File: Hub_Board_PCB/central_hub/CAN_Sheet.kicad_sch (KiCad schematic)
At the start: 14 parts, among them J6 CAN_OUT, U1 MCP2515-xST, U2 TJA1050, Y1 20M

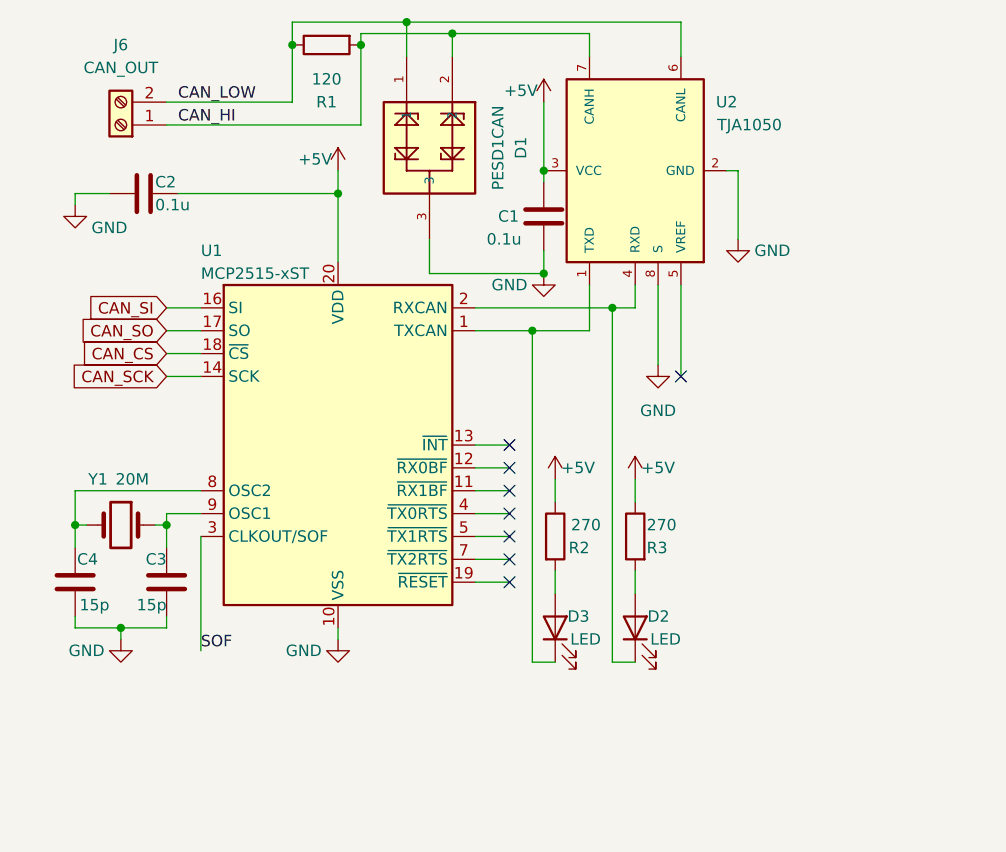
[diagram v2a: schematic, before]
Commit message: Added footprints for almost all components
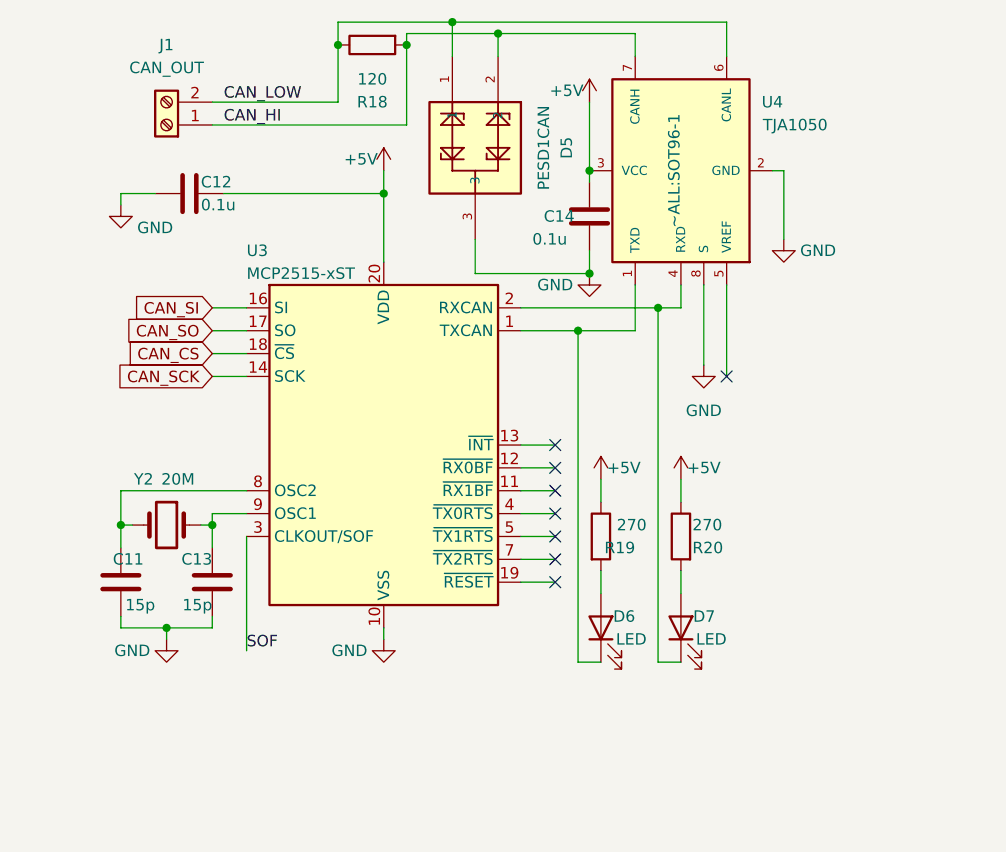
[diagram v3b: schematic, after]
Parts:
- removed C1, C2: 0.1u, Capacitor_SMD:C_0603_1608Metric, symbol Device:C
- removed C3, C4: 15p, Capacitor_SMD:C_0603_1608Metric, symbol Device:C
- removed D1: PESD1CAN, PESD1CAN:SOT23-3, symbol PESD1CAN:PESD1CAN
- removed D2, D3: LED, LED_SMD:LED_1206_3216Metric, symbol Device:LED
- removed J6: CAN_OUT, symbol Connector:Screw_Terminal_01x02
- removed R1: 120, Resistor_SMD:R_0603_1608Metric_Pad0.98x0.95mm_HandSolder, symbol Device:R
- removed R2, R3: 270, Resistor_SMD:R_0603_1608Metric_Pad0.98x0.95mm_HandSolder, symbol Device:R
- removed U1: MCP2515-xST, Package_SO:TSSOP-20_4.4x6.5mm_P0.65mm, symbol Interface_CAN_LIN:MCP2515-xST
- removed U2: TJA1050, TJA1050:SOT96-1, symbol TJA1050:TJA1050
- removed Y1: 20M, Crystal:Crystal_HC49-U_Vertical, symbol Device:Crystal
- added C11, C13: 15p, Capacitor_SMD:C_0603_1608Metric, symbol Device:C
- added C12, C14: 0.1u, Capacitor_SMD:C_0603_1608Metric, symbol Device:C
- added D5: PESD1CAN, ~ALL:SOT23-3, symbol PESD1CAN:PESD1CAN
- added D6, D7: LED, LED_SMD:LED_1206_3216Metric, symbol Device:LED
- added J1: CAN_OUT, Connector_PinHeader_2.54mm:PinHeader_1x02_P2.54mm_Vertical, symbol Connector:Screw_Terminal_01x02
- added R18: 120, Resistor_SMD:R_0603_1608Metric_Pad0.98x0.95mm_HandSolder, symbol Device:R
- added R19, R20: 270, Resistor_SMD:R_0603_1608Metric_Pad0.98x0.95mm_HandSolder, symbol Device:R
- added U3: MCP2515-xST, Package_SO:TSSOP-20_4.4x6.5mm_P0.65mm, symbol Interface_CAN_LIN:MCP2515-xST
- added U4: TJA1050, ~ALL:SOT96-1, symbol TJA1050:TJA1050
- added Y2: 20M, Crystal:Crystal_HC49-U_Vertical, symbol Device:Crystal
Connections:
- net +5V: now also C12.1, C14.1, R19.1, R20.1, U3.20 (VDD), U4.3 (VCC)
- net CAN_CS: now also U3.18 (~{CS})
- net CAN_HI: now also D5.2, J1.1 (Pin_1), R18.2, U4.7 (CANH)
- net CAN_LOW: now also D5.1, J1.2 (Pin_2), R18.1, U4.6 (CANL)
- net CAN_SCK: now also U3.14 (SCK)
- net CAN_SI: now also U3.16 (SI)
- net CAN_SO: now also U3.17 (SO)
- net GND: now also C11.1, C12.2, C13.1, C14.2, D5.3, U3.10 (VSS), U4.2 (GND), U4.8 (S)
- net SOF: now also U3.3 (CLKOUT/SOF)
- new net: D6.1 (K), U3.1 (TXCAN), U4.1 (TXD)
- new net: D7.1 (K), U3.2 (RXCAN), U4.4 (RXD)
- new net: D7.2 (A), R20.2
- new net: C13.2, U3.9 (OSC1), Y2.1
- new net: C11.2, U3.8 (OSC2), Y2.2
- new net: D6.2 (A), R19.2

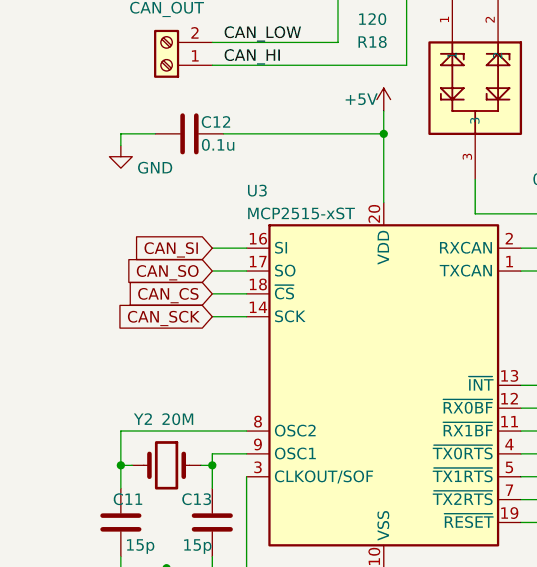
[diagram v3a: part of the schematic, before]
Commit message: Started Layout (hub board)
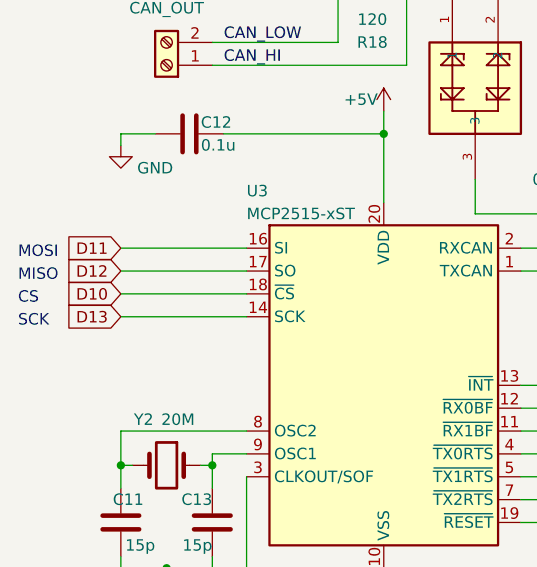
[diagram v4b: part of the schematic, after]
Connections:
- net CAN_CS renamed D10
- net CAN_SCK renamed D13
- net CAN_SI renamed D11
- net CAN_SO renamed D12
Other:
- note added: "CS"
- note added: "MISO"
- note added: "MOSI"
- note added: "SCK"
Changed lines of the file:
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@@
     (stroke (width 0) (type default))
   )
-  (wire (pts (xy 38.1 59.69) (xy 41.91 59.69))
+  (wire (pts (xy 27.94 59.69) (xy 41.91 59.69))
     (stroke (width 0) (type default))
   )
@@
     (stroke (width 0) (type default))
   )
-  (wire (pts (xy 38.1 54.61) (xy 41.91 54.61))
+  (wire (pts (xy 27.94 54.61) (xy 41.91 54.61))
     (stroke (width 0) (type default))
   )
-  (wire (pts (xy 38.1 52.07) (xy 41.91 52.07))
+  (wire (pts (xy 27.94 52.07) (xy 41.91 52.07))
     (stroke (width 0) (type default))
   )
@@
     (stroke (width 0) (type default))
   )
-  (wire (pts (xy 38.1 57.15) (xy 41.91 57.15))
+  (wire (pts (xy 27.94 57.15) (xy 41.91 57.15))
     (stroke (width 0) (type default))
   )
   (wire (pts (xy 33.02 87.63) (xy 33.02 88.9))
     (stroke (width 0) (type default))
+  )
+  (text "MOSI" (at 16.51 53.34 0)
+    (effects (font (size 1.27 1.27)) (justify left bottom))
+  )
+  (text "MISO\n" (at 16.51 55.88 0)
+    (effects (font (size 1.27 1.27)) (justify left bottom))
+  )
+  (text "SCK\n" (at 16.51 60.96 0)
+    (effects (font (size 1.27 1.27)) (justify left bottom))
+  )
+  (text "CS" (at 16.51 58.42 0)
+    (effects (font (size 1.27 1.27)) (justify left bottom))
   )
   (label "CAN_LOW" (at 39.37 29.21 0) (fields_autoplaced)
@@
     (effects (font (size 1.27 1.27)) (justify left bottom))
   )
-  (global_label "CAN_SCK" (shape input) (at 38.1 59.69 180) (fields_autoplaced)
+  (global_label "D11" (shape input) (at 27.94 52.07 180) (fields_autoplaced)
     (effects (font (size 1.27 1.27)) (justify right))
-    (property "Intersheetrefs" "${INTERSHEET_REFS}" (at 26.0589 59.69 0)
+    (property "Intersheetrefs" "${INTERSHEET_REFS}" (at 21.4252 52.07 0)
       (effects (font (size 1.27 1.27)) (justify right) hide)
     )
   )
-  (global_label "CAN_CS" (shape input) (at 38.1 57.15 180) (fields_autoplaced)
+  (global_label "D12" (shape input) (at 27.94 54.61 180) (fields_autoplaced)
     (effects (font (size 1.27 1.27)) (justify right))
-    (property "Intersheetrefs" "${INTERSHEET_REFS}" (at 27.5391 57.15 0)
+    (property "Intersheetrefs" "${INTERSHEET_REFS}" (at 21.4252 54.61 0)
       (effects (font (size 1.27 1.27)) (justify right) hide)
     )
   )
-  (global_label "CAN_SO" (shape input) (at 38.1 54.61 180) (fields_autoplaced)
+  (global_label "D13" (shape input) (at 27.94 59.69 180) (fields_autoplaced)
     (effects (font (size 1.27 1.27)) (justify right))
-    (property "Intersheetrefs" "${INTERSHEET_REFS}" (at 27.4411 54.61 0)
+    (property "Intersheetrefs" "${INTERSHEET_REFS}" (at 21.4252 59.69 0)
       (effects (font (size 1.27 1.27)) (justify right) hide)
     )
   )
-  (global_label "CAN_SI" (shape input) (at 38.1 52.07 180) (fields_autoplaced)
+  (global_label "D10" (shape input) (at 27.94 57.15 180) (fields_autoplaced)
     (effects (font (size 1.27 1.27)) (justify right))
-    (property "Intersheetrefs" "${INTERSHEET_REFS}" (at 28.2302 52.07 0)
+    (property "Intersheetrefs" "${INTERSHEET_REFS}" (at 21.4252 57.15 0)
       (effects (font (size 1.27 1.27)) (justify right) hide)
     )

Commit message: Schematic changes before sending to kim
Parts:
- added TP11: TestPoint, TestPoint:TestPoint_Pad_D1.0mm, symbol Connector:TestPoint
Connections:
- net at U3.19 (~{RESET}): now also TP11.1
- no-connect marks 8 -> 7
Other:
- moved on the sheet: C11, C12, C13, C14, D5, D6, D7, R19, R20, U3, U4, Y2

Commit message: Meeting layout updates
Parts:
- added R7: 0, Resistor_SMD:R_0402_1005Metric, symbol Device:R
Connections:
- net D12: now also R7.2; no longer U3.17 (SO)
- new net: R7.1, U3.17 (SO)
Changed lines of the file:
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@@
   (no_connect (at 76.2 87.63))
   (no_connect (at 76.2 82.55))
+  (wire (pts (xy 27.94 69.85) (xy 31.75 69.85))
+    (stroke (width 0) (type default))
+  )
   (wire (pts (xy 27.94 54.61) (xy 27.94 55.88))
     (stroke (width 0) (type default))
@@
     (stroke (width 0) (type default))
   )
+  (wire (pts (xy 39.37 69.85) (xy 41.91 69.85))
+    (stroke (width 0) (type default))
+  )
   (wire (pts (xy 92.71 67.31) (xy 92.71 107.95))
     (stroke (width 0) (type default))
@@
   )
   (wire (pts (xy 93.98 45.72) (xy 93.98 48.26))
-    (stroke (width 0) (type default))
-  )
-  (wire (pts (xy 27.94 69.85) (xy 41.91 69.85))
     (stroke (width 0) (type default))
   )
@@
         )
       )
+    )
+  )
+  (symbol (lib_id "Device:R") (at 35.56 69.85 270) (unit 1)
+    (in_bom yes) (on_board yes) (dnp no)
+    (property "Reference" "R7" (at 35.56 76.2 90)
+      (effects (font (size 1.27 1.27)))
+    )
+    (property "Value" "0" (at 35.56 73.66 90)
+      (effects (font (size 1.27 1.27)))
+    )
+    (property "Footprint" "Resistor_SMD:R_0402_1005Metric" (at 35.56 68.072 90)
+      (effects (font (size 1.27 1.27)) hide)
+    )
+    (property "Datasheet" "~" (at 35.56 69.85 0)
+      (effects (font (size 1.27 1.27)) hide)
+    )
+    (pin "1")
+    (pin "2")
+    (instances
+      (project "central_hub"
+        (path "/0d9ec66e-0fbf-4d12-9b83-adf78971a00b/a9a7affa-d8a7-4dcd-8fe3-0de6a2b29bd6"
+          (reference "R7") (unit 1)
+        )
+      )
+      (project "motor_board_pcb"
+        (path "/4ad82a24-c992-45c9-b523-12e12bcd6ced"
+          (reference "R?") (unit 1)
+        )
+        (path "/4ad82a24-c992-45c9-b523-12e12bcd6ced/63c66207-e5d4-4f6f-af8f-451675dc3930"
+          (reference "R16") (unit 1)
+        )
+      )

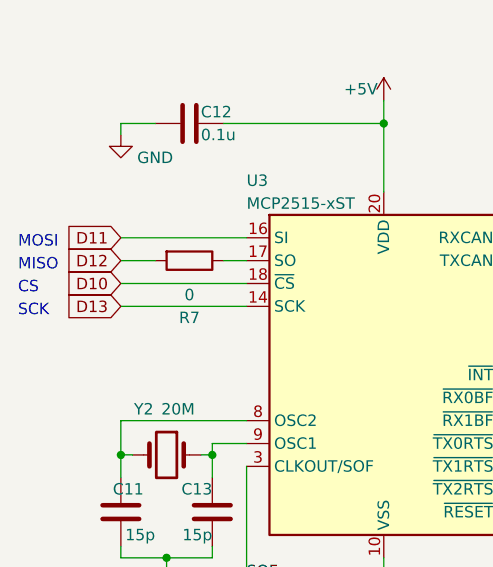
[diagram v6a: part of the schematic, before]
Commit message: added additional cs pin for display/can
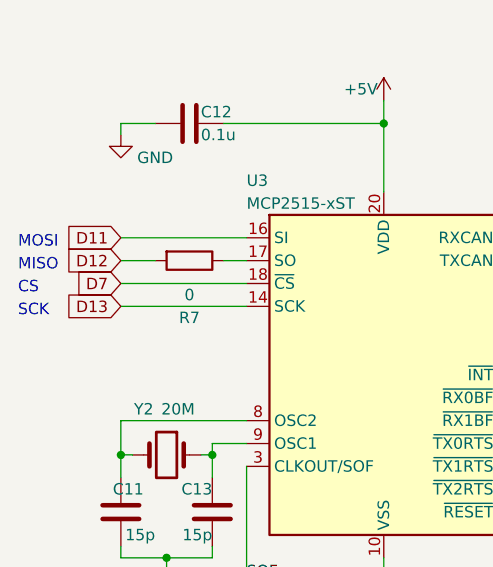
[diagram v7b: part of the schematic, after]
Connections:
- net D10 renamed D7
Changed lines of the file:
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@@
     )
   )
-  (global_label "D10" (shape input) (at 27.94 72.39 180) (fields_autoplaced)
+  (global_label "D7" (shape input) (at 27.94 72.39 180) (fields_autoplaced)
     (effects (font (size 1.27 1.27)) (justify right))
-    (property "Intersheetrefs" "${INTERSHEET_REFS}" (at 21.4252 72.39 0)
+    (property "Intersheetrefs" "${INTERSHEET_REFS}" (at 22.4753 72.39 0)
       (effects (font (size 1.27 1.27)) (justify right) hide)
     )

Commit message: Kim changes
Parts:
- added C32: 0.1u, Capacitor_SMD:C_0402_1005Metric, symbol Device:C
- added R11: 0, Resistor_SMD:R_0402_1005Metric, symbol Device:R
- C11, C13: value 15p -> 22p
- Y2: value 20M -> 8M
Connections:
- net D13: now also R11.2; no longer U3.14 (SCK)
- net GND: now also C32.2
- new net: C32.1, R11.1, U3.14 (SCK)
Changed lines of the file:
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@@
   (junction (at 93.98 48.26) (diameter 0) (color 0 0 0 0)
+  )
+  (junction (at 38.1 74.93) (diameter 0) (color 0 0 0 0)
   )
   (junction (at 57.15 54.61) (diameter 0) (color 0 0 0 0)
@@
     (stroke (width 0) (type default))
   )
-  (wire (pts (xy 27.94 74.93) (xy 41.91 74.93))
+  (wire (pts (xy 27.94 74.93) (xy 29.21 74.93))
     (stroke (width 0) (type default))
   )
@@
     (stroke (width 0) (type default))
   )
+  (wire (pts (xy 36.83 74.93) (xy 38.1 74.93))
+    (stroke (width 0) (type default))
+  )
   (wire (pts (xy 72.39 85.09) (xy 76.2 85.09))
     (stroke (width 0) (type default))
@@
     (stroke (width 0) (type default))
   )
+  (wire (pts (xy 38.1 74.93) (xy 41.91 74.93))
+    (stroke (width 0) (type default))
+  )
   (wire (pts (xy 41.91 92.71) (xy 41.91 105.41))
     (stroke (width 0) (type default))
@@
   )
   (wire (pts (xy 72.39 92.71) (xy 76.2 92.71))
+    (stroke (width 0) (type default))
+  )
+  (wire (pts (xy 38.1 74.93) (xy 38.1 76.2))
     (stroke (width 0) (type default))
   )
@@
     (property "Intersheetrefs" "${INTERSHEET_REFS}" (at 22.4753 72.39 0)
       (effects (font (size 1.27 1.27)) (justify right) hide)
+    )
+  )
+  (symbol (lib_id "power:GND") (at 38.1 83.82 0) (unit 1)
+    (in_bom yes) (on_board yes) (dnp no)
+    (property "Reference" "#PWR01" (at 38.1 90.17 0)
+      (effects (font (size 1.27 1.27)) hide)
+    )
+    (property "Value" "GND" (at 41.91 83.82 0)
+      (effects (font (size 1.27 1.27)))
+    )
+    (property "Footprint" "" (at 38.1 83.82 0)
+      (effects (font (size 1.27 1.27)) hide)
+    )
+    (property "Datasheet" "" (at 38.1 83.82 0)
+      (effects (font (size 1.27 1.27)) hide)
+    )
+    (pin "1")
+    (instances
+      (project "central_hub"
+        (path "/0d9ec66e-0fbf-4d12-9b83-adf78971a00b/a9a7affa-d8a7-4dcd-8fe3-0de6a2b29bd6"
+          (reference "#PWR01") (unit 1)
+        )
+      )
+      (project "motor_board_pcb"
+        (path "/4ad82a24-c992-45c9-b523-12e12bcd6ced"
+          (reference "#PWR?") (unit 1)
+        )
+        (path "/4ad82a24-c992-45c9-b523-12e12bcd6ced/63c66207-e5d4-4f6f-af8f-451675dc3930"
+          (reference "#PWR031") (unit 1)
+        )
+      )
     )
   )
@@
       (effects (font (size 1.27 1.27)) (justify left))
     )
-    (property "Value" "15p" (at 38.1 100.33 0)
+    (property "Value" "22p" (at 38.1 100.33 0)
       (effects (font (size 1.27 1.27)) (justify left))
     )
@@
       (effects (font (size 1.27 1.27)) (justify left))
     )
-    (property "Value" "15p" (at 31.75 100.33 0)
+    (property "Value" "22p" (at 31.75 100.33 0)
       (effects (font (size 1.27 1.27)) (justify left))
     )
@@
         (path "/4ad82a24-c992-45c9-b523-12e12bcd6ced/63c66207-e5d4-4f6f-af8f-451675dc3930"
           (reference "C11") (unit 1)
+        )
+      )
+    )
+  )
+  (symbol (lib_id "Device:R") (at 33.02 74.93 270) (unit 1)
+    (in_bom yes) (on_board yes) (dnp no)
+    (property "Reference" "R11" (at 33.02 81.28 90)
+      (effects (font (size 1.27 1.27)))
+    )
+    (property "Value" "0" (at 33.02 78.74 90)
+      (effects (font (size 1.27 1.27)))
+    )
+    (property "Footprint" "Resistor_SMD:R_0402_1005Metric" (at 33.02 73.152 90)
+      (effects (font (size 1.27 1.27)) hide)
+    )
+    (property "Datasheet" "~" (at 33.02 74.93 0)
+      (effects (font (size 1.27 1.27)) hide)
+    )
+    (pin "1")
+    (pin "2")
+    (instances
+      (project "central_hub"
+        (path "/0d9ec66e-0fbf-4d12-9b83-adf78971a00b/a9a7affa-d8a7-4dcd-8fe3-0de6a2b29bd6"
+          (reference "R11") (unit 1)
+        )
+      )
+      (project "motor_board_pcb"
+        (path "/4ad82a24-c992-45c9-b523-12e12bcd6ced"
+          (reference "R?") (unit 1)
+        )
+        (path "/4ad82a24-c992-45c9-b523-12e12bcd6ced/63c66207-e5d4-4f6f-af8f-451675dc3930"
+          (reference "R16") (unit 1)
         )
       )
@@
     )
   )
+  (symbol (lib_id "Device:C") (at 38.1 80.01 0) (unit 1)
+    (in_bom yes) (on_board yes) (dnp no)
+    (property "Reference" "C32" (at 36.83 78.74 90)
+      (effects (font (size 1.27 1.27)) (justify left))
+    )
+    (property "Value" "0.1u" (at 39.37 78.74 90)
+      (effects (font (size 1.27 1.27)) (justify left))
+    )
+    (property "Footprint" "Capacitor_SMD:C_0402_1005Metric" (at 39.0652 83.82 0)
+      (effects (font (size 1.27 1.27)) hide)
+    )
+    (property "Datasheet" "~" (at 38.1 80.01 0)
+      (effects (font (size 1.27 1.27)) hide)
+    )
+    (pin "1")
+    (pin "2")
+    (instances
+      (project "central_hub"
+        (path "/0d9ec66e-0fbf-4d12-9b83-adf78971a00b/a9a7affa-d8a7-4dcd-8fe3-0de6a2b29bd6"
+          (reference "C32") (unit 1)
+        )
+      )
+      (project "motor_board_pcb"
+        (path "/4ad82a24-c992-45c9-b523-12e12bcd6ced"
+          (reference "C?") (unit 1)
+        )
+        (path "/4ad82a24-c992-45c9-b523-12e12bcd6ced/63c66207-e5d4-4f6f-af8f-451675dc3930"
+          (reference "C12") (unit 1)
+        )
+      )
+    )
+  )
   (symbol (lib_id "power:+5V") (at 85.09 86.36 0) (unit 1)
     (in_bom yes) (on_board yes) (dnp no)
@@
       (effects (font (size 1.27 1.27)))
     )
-    (property "Value" "20M" (at 34.29 86.36 0)
-      (effects (font (size 1.27 1.27)))
-    )
+    (property "Value" "8M" (at 34.29 86.36 0)
+      (effects (font (size 1.27 1.27)))
+    )
